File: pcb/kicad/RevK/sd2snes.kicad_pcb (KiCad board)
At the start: 2 copper layers, 101.5 x 83 mm, 148 parts, among them J101 SNESCART_EXT, J411 Hirose DM1AA, J421 USB Mini-B SMT, P113 CONN_1, P401 CONN_7X2, P402 CONN_2, P403 CONN_2, P404 CONN_3X2, Q101 2N2222A, Q301 IRLML6402PbF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

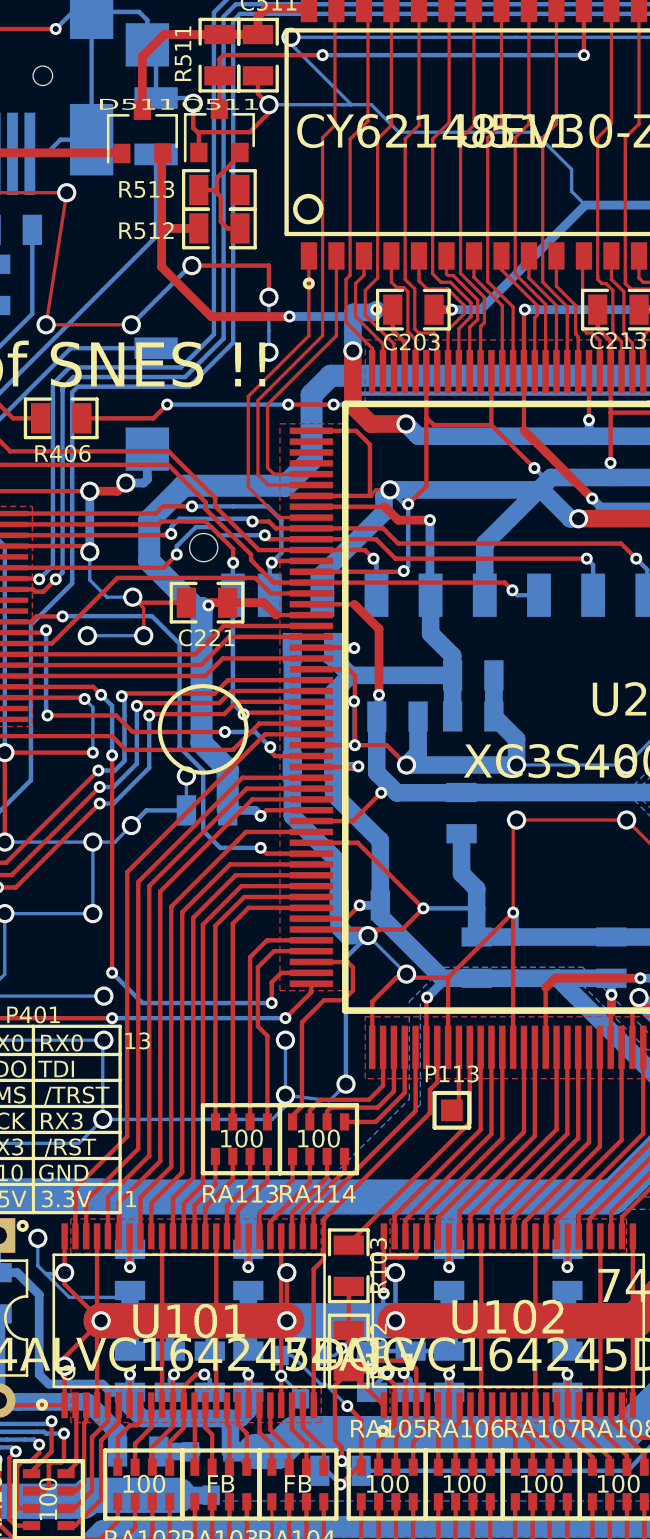
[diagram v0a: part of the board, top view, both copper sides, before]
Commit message: Fixes for Transistor placement
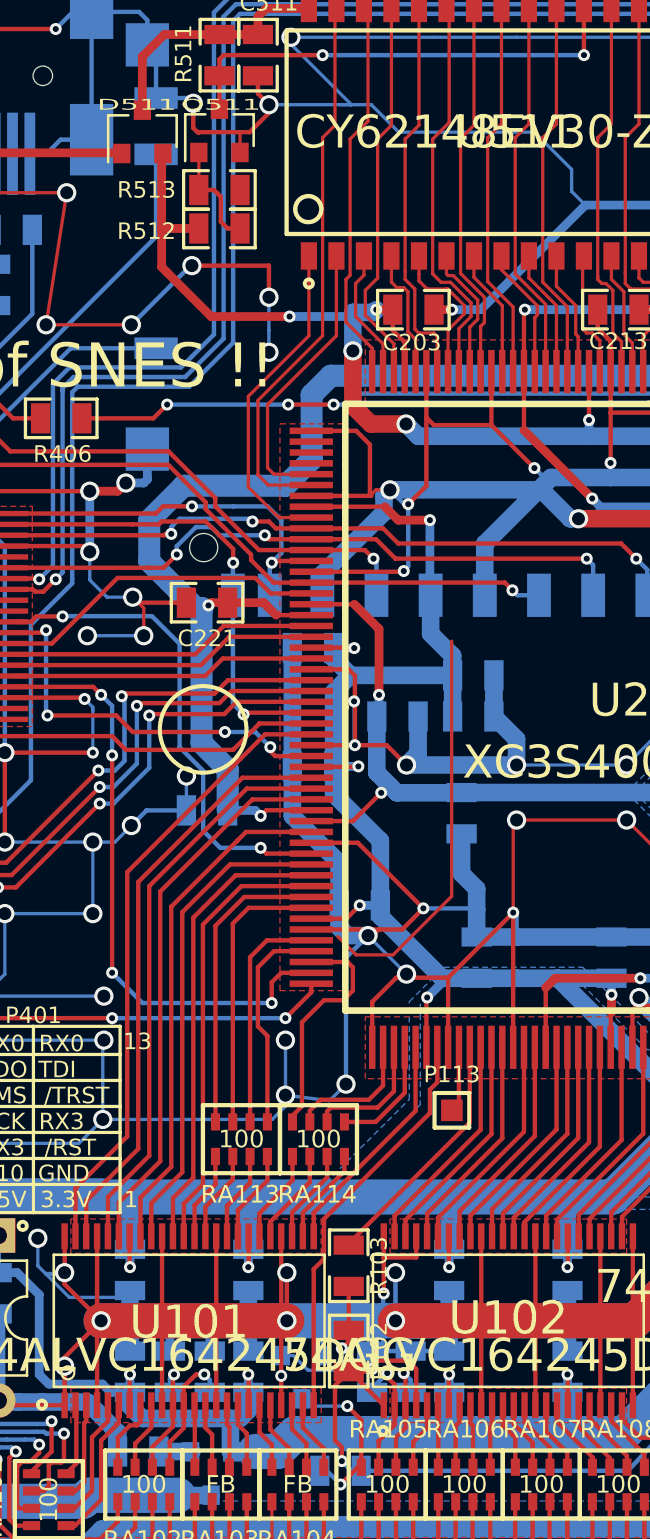
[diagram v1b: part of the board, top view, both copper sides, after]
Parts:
- moved Q101 0.06 mm to (142.5, 119.7)
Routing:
- net GND: track 1916.9 -> 1935.7 mm
- net Net-(Q101-Pad2): track 4.08 -> 6.89 mm
- net Net-(C123-Pad1): track 9.67 -> 8.00 mm
- net Net-(Q511-Pad2): track 5.66 -> 5.13 mm
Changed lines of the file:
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@@
     (thickness 0.8)
     (drawings 242)
-    (tracks 4097)
+    (tracks 4110)
     (zones 0)
     (modules 148)
@@
   )
   (layers
-    (0 Component signal)
-    (31 Copper signal hide)
+    (0 Component signal hide)
+    (31 Copper signal)
     (32 B.Adhes user hide)
     (33 F.Adhes user hide)
@@
   )
   (setup
-    (last_trace_width 0.2032)
+    (last_trace_width 0.1524)
     (user_trace_width 0.14986)
     (user_trace_width 0.1524)
@@
   )
   (module mypackages:SOT-23-EBC (layer Copper)
-    (at 142.4305 119.6975 270)
+    (at 142.494 119.6975 270)
     (descr "SOT-23, Standard")
     (tags SOT-23)
@@
   (segment (start 133.731 90.1065) (end 126.8095 90.1065) (width 0.2032) (layer Component) (net 86))
   (segment (start 142.9258 89.52484) (end 140.53058 89.52484) (width 0.2032) (layer Component) (net 86) (status 800))
+  (segment (start 144.994611 100.20299) (end 144.153891 99.36227) (width 0.1524) (layer Component) (net 87))
+  (segment (start 146.699033 100.20299) (end 144.994611 100.20299) (width 0.1524) (layer Component) (net 87))
+  (segment (start 149.4028 85.725) (end 149.4028 97.499223) (width 0.1524) (layer Component) (net 87))
+  (segment (start 149.4028 97.499223) (end 146.699033 100.20299) (width 0.1524) (layer Component) (net 87))
   (segment (start 119.888 127.6096) (end 132.4864 127.6096) (width 1.016) (layer Copper) (net 87))
   (segment (start 119.888 127.6096) (end 119.888 124.968) (width 1.016) (layer Component) (net 87))
@@
   (segment (start 101.9175 94.2975) (end 101.9175 99.568) (width 0.2032) (layer Component) (net 87))
   (via (at 118.364 113.03) (size 0.889) (drill 0.59944) (layers Component Copper) (net 87))
-  (segment (start 140.081 62.23) (end 139.3825 62.23) (width 0.2032) (layer Component) (net 87))
   (segment (start 99.1235 100.33) (end 97.79 100.33) (width 0.2032) (layer Component) (net 87) (status 400))
   (via (at 186.436 71.12) (size 0.889) (drill 0.59944) (layers Component Copper) (net 87))
@@
   (segment (start 120.8532 90.4875) (end 118.999 90.4875) (width 0.2032) (layer Component) (net 87))
   (segment (start 137.668 62.23) (end 137.734 62.296) (width 0.1524) (layer Component) (net 87))
-  (segment (start 137.734 63.23) (end 137.734 62.296) (width 0.2032) (layer Component) (net 87))
   (segment (start 141.53642 119.634) (end 141.53642 117.35308) (width 0.2032) (layer Component) (net 87) (status 800))
   (via (at 141.53642 119.634) (size 0.55372) (drill 0.29972) (layers Component Copper) (net 87))
-  (segment (start 142.4305 120.52808) (end 141.53642 119.634) (width 0.1524) (layer Copper) (net 87))
-  (segment (start 142.4305 120.6975) (end 142.4305 120.52808) (width 0.1524) (layer Copper) (net 87))
+  (segment (start 142.4305 120.6975) (end 142.4305 120.52808) (width 0.1524) (layer Copper) (net 306))
+  (segment (start 139.634 63.28) (end 139.634 63.23) (width 0.2032) (layer Component) (net 87))
+  (segment (start 139.6492 62.23) (end 139.3825 62.23) (width 0.2032) (layer Component) (net 87))
+  (segment (start 139.634 62.2452) (end 139.634 63.1665) (width 0.1524) (layer Component) (net 87))
+  (segment (start 139.6492 62.23) (end 139.634 62.2452) (width 0.1524) (layer Component) (net 87))
+  (segment (start 140.081 62.23) (end 139.6492 62.23) (width 0.2032) (layer Component) (net 87))
+  (segment (start 143.1925 117.8436) (end 143.1925 117.094) (width 0.1524) (layer Copper) (net 87))
+  (segment (start 143.444 118.0951) (end 143.1925 117.8436) (width 0.1524) (layer Copper) (net 87))
+  (segment (start 143.444 118.6975) (end 143.444 118.0951) (width 0.1524) (layer Copper) (net 87))
   (segment (start 130.683 85.217) (end 130.5687 85.3313) (width 0.2032) (layer Component) (net 88))
   (segment (start 130.7465 89.154) (end 130.683 89.0905) (width 0.2032) (layer Copper) (net 88))
@@
   (segment (start 138.5824 65.0494) (end 138.43 64.897) (width 0.2032) (layer Component) (net 305))
   (segment (start 138.7475 65.2145) (end 138.5824 65.0494) (width 0.2032) (layer Component) (net 305))
-  (segment (start 138.5824 64.3316) (end 139.634 63.28) (width 0.2032) (layer Component) (net 305))
-  (segment (start 139.634 63.28) (end 139.634 63.23) (width 0.2032) (layer Component) (net 305))
-  (segment (start 138.5824 65.0494) (end 138.5824 64.3316) (width 0.2032) (layer Component) (net 305))
+  (segment (start 137.734 64.8945) (end 137.7315 64.897) (width 0.1524) (layer Component) (net 305))
+  (segment (start 137.734 63.1665) (end 137.734 64.8945) (width 0.1524) (layer Component) (net 305))
   (segment (start 145.06956 123.85294) (end 145.23212 123.85294) (width 0.2032) (layer Component) (net 306))
   (segment (start 144.5895 121.031) (end 145.23212 121.67362) (width 0.2032) (layer Component) (net 306))
@@
   (segment (start 144.77238 124.15012) (end 145.06956 123.85294) (width 0.2032) (layer Component) (net 306))
   (via (at 144.5895 121.031) (size 0.55372) (layers Component Copper) (net 306))
-  (segment (start 142.0329 118.6975) (end 141.4805 118.6975) (width 0.1524) (layer Copper) (net 306))
-  (segment (start 143.354299 120.018899) (end 142.0329 118.6975) (width 0.1524) (layer Copper) (net 306))
-  (segment (start 143.577399 120.018899) (end 143.354299 120.018899) (width 0.1524) (layer Copper) (net 306))
-  (segment (start 144.5895 121.031) (end 143.577399 120.018899) (width 0.1524) (layer Copper) (net 306))
+  (segment (start 142.8275 121.031) (end 142.494 120.6975) (width 0.1524) (layer Copper) (net 306))
+  (segment (start 144.5895 121.031) (end 142.8275 121.031) (width 0.1524) (layer Copper) (net 306))
   (via (at 144.3355 118.364) (size 0.55372) (layers Component Copper) (net 307))
   (segment (start 144.653 118.0465) (end 144.653 117.5385) (width 0.2032) (layer Component) (net 307) (status 400))
   (segment (start 144.653 118.0465) (end 144.3355 118.364) (width 0.2032) (layer Component) (net 307))
   (segment (start 144.653 115.5065) (end 144.653 117.5385) (width 0.2032) (layer Component) (net 307) (status C00))
-  (segment (start 144.002 118.6975) (end 144.3355 118.364) (width 0.1524) (layer Copper) (net 307))
-  (segment (start 143.3805 118.6975) (end 144.002 118.6975) (width 0.1524) (layer Copper) (net 307))
+  (segment (start 144.3355 118.755539) (end 144.3355 118.364) (width 0.1524) (layer Copper) (net 307))
+  (segment (start 144.026881 119.376101) (end 144.3355 119.067482) (width 0.1524) (layer Copper) (net 307))
+  (segment (start 144.3355 119.067482) (end 144.3355 118.755539) (width 0.1524) (layer Copper) (net 307))
+  (segment (start 142.775001 119.376101) (end 144.026881 119.376101) (width 0.1524) (layer Copper) (net 307))
+  (segment (start 142.0964 118.6975) (end 142.775001 119.376101) (width 0.1524) (layer Copper) (net 307))
+  (segment (start 141.544 118.6975) (end 142.0964 118.6975) (width 0.1524) (layer Copper) (net 307))
   (segment (start 122.35942 105.66908) (end 122.35942 91.5797) (width 0.2032) (layer Component) (net 310) (status 400))
   (segment (start 121.7295 106.299) (end 122.35942 105.66908) (width 0.2032) (layer Component) (net 310))
@@
   (via (at 127.5715 75.2475) (size 0.55372) (layers Component Copper) (net 334))
   (segment (start 127.5715 75.2475) (end 126.1745 75.2475) (width 0.2032) (layer Component) (net 334))
-  (segment (start 101.944 111.9915) (end 101.444 111.9915) (width 0.2032) (layer Component) (net 344))
-  (segment (start 103.76916 107.6579) (end 103.76916 110.16634) (width 0.2032) (layer Component) (net 345))
-  (segment (start 105.26522 107.6579) (end 105.26522 111.49092) (width 0.2032) (layer Component) (net 346))
   (segment (start 106.299 115.4303) (end 106.299 116.332) (width 0.2032) (layer Component) (net 343))
   (segment (start 108.310202 112.701202) (end 108.259401 112.650401) (width 0.2032) (layer Component) (net 343))
@@
   (segment (start 107.258504 115.4303) (end 108.310202 114.378602) (width 0.2032) (layer Component) (net 343))
   (segment (start 106.299 115.4303) (end 107.258504 115.4303) (width 0.2032) (layer Component) (net 343))
+  (segment (start 101.944 111.9915) (end 101.444 111.9915) (width 0.2032) (layer Component) (net 344))
   (segment (start 100.584 116.078) (end 100.584 116.332) (width 0.2032) (layer Component) (net 344))
   (segment (start 102.423001 114.492999) (end 100.584 116.332) (width 0.2032) (layer Component) (net 344))
@@
   (segment (start 102.423001 112.064001) (end 102.359401 112.000401) (width 0.2032) (layer Component) (net 344))
   (segment (start 102.423001 114.492999) (end 102.423001 112.064001) (width 0.2032) (layer Component) (net 344))
+  (segment (start 103.76916 107.6579) (end 103.76916 110.16634) (width 0.2032) (layer Component) (net 345))
   (segment (start 101.431201 113.300401) (end 101.431201 112.650401) (width 0.2032) (layer Component) (net 345))
   (segment (start 101.94906 110.16634) (end 103.76916 110.16634) (width 0.2032) (layer Component) (net 345))
@@
   (segment (start 100.503001 112.650401) (end 100.4522 112.5996) (width 0.2032) (layer Component) (net 345))
   (segment (start 101.431201 112.650401) (end 100.503001 112.650401) (width 0.2032) (layer Component) (net 345))
+  (segment (start 105.26522 107.6579) (end 105.26522 111.49092) (width 0.2032) (layer Component) (net 346))
   (segment (start 107.331201 113.950401) (end 107.331201 113.300401) (width 0.2032) (layer Component) (net 346))
   (segment (start 106.403001 113.300401) (end 105.26522 112.16262) (width 0.2032) (layer Component) (net 346))

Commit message: Fix stupid layout mistake
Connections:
- U230 pad 2: Net-(U230-Pad2) -> Net-(R231-Pad1)
- U230 pad 3: Net-(U230-Pad2) -> Net-(U230-Pad3)
- U230 pad 6: Net-(U230-Pad5) -> Net-(R230-Pad1)
- U341 pad 7: Net-(U230-Pad2) -> Net-(U230-Pad3)
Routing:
- net Net-(U230-Pad2): track 9.03 -> 0.00 mm
- net Net-(U230-Pad3): track 0.00 -> 7.15 mm
- net GNDA: track 106.7 -> 104.5 mm
- net Net-(R231-Pad1): track 6.80 -> 6.18 mm

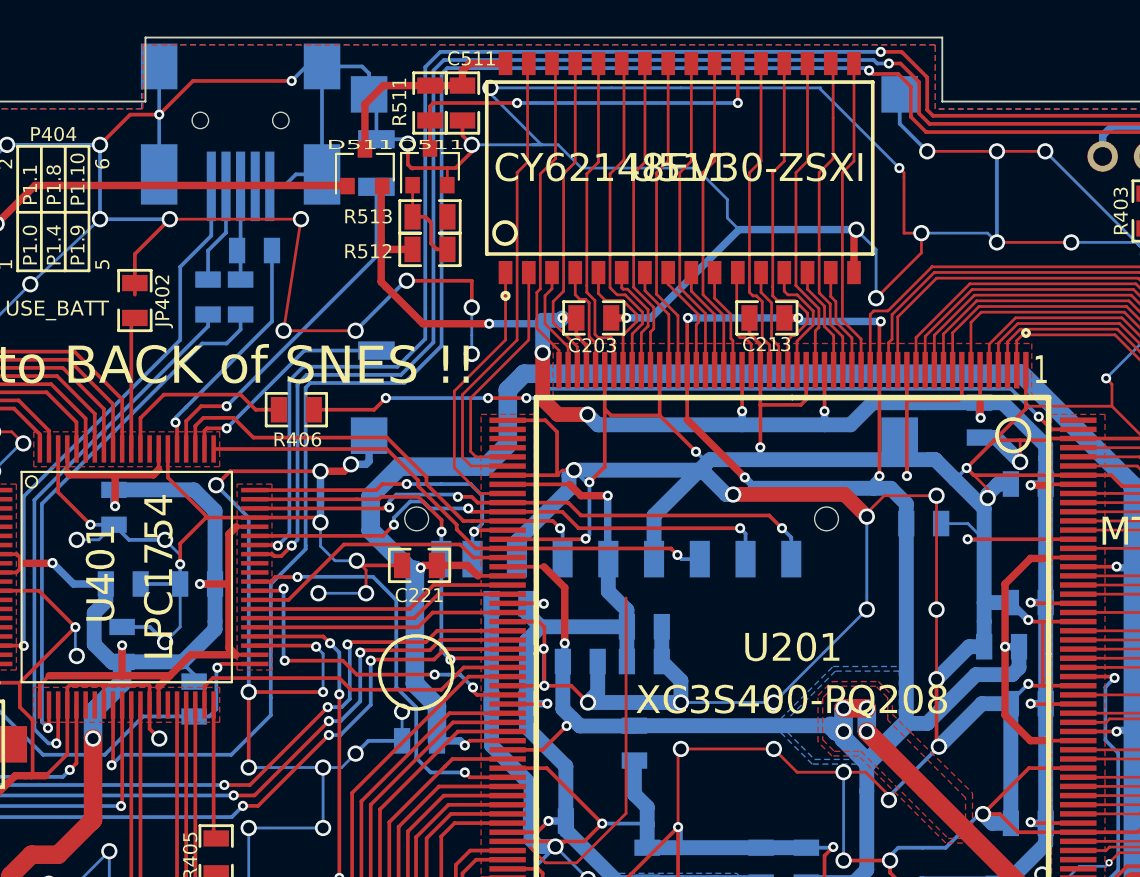
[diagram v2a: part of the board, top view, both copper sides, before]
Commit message: - Reroute to use small SD card slot
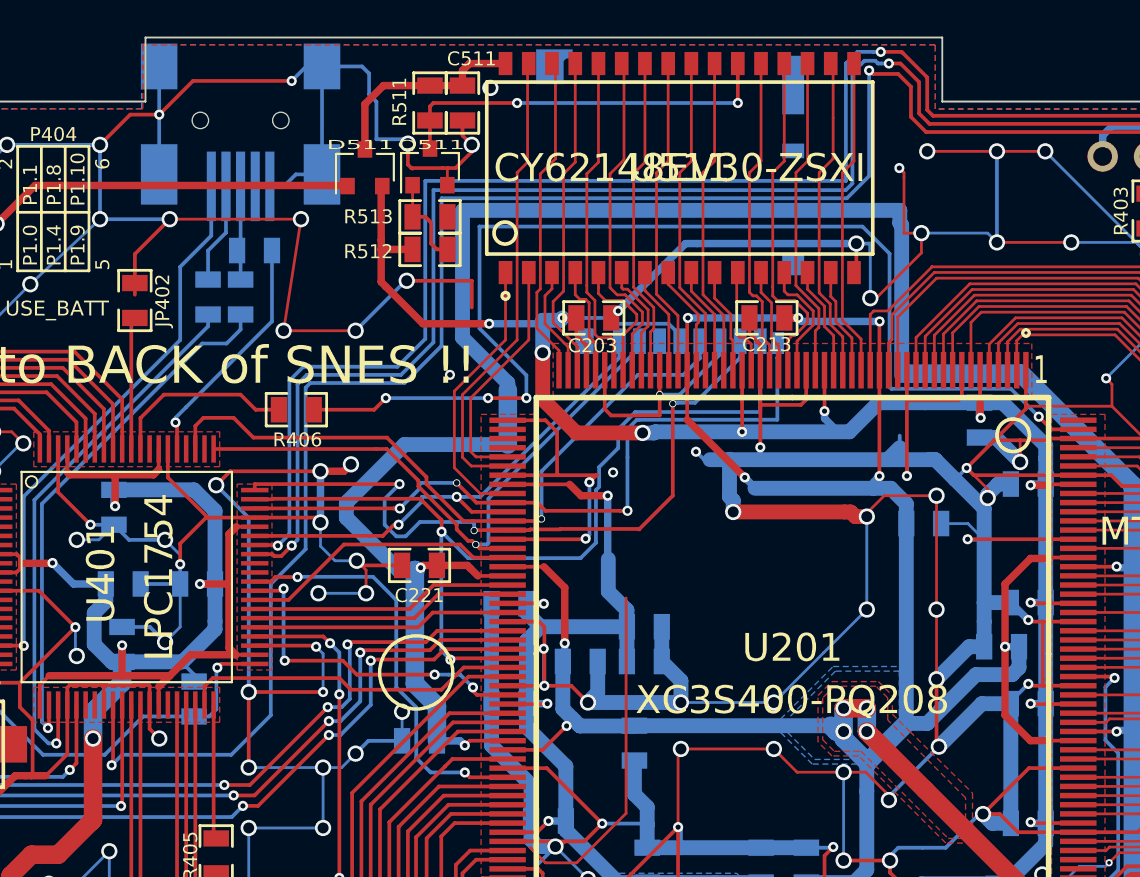
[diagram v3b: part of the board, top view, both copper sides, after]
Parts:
- J411: footprint mypackages:HRS-DM1AA -> Connectors_Card:Hirose_DM3BT-DSF-PEJS
- moved J411 2.43 mm to (149.0, 71.0)
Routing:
- net GND: track 1935.7 -> 1857.4 mm
- net SD_DAT1: track 21.8 -> 49.8 mm
- net +1.2V: track 115.5 -> 139.2 mm
- net SD_DAT0: track 18.4 -> 39.4 mm, vias 2 -> 3
- net PROG_B: track 43.2 -> 64.0 mm
- net Net-(J411-PadWP): track 19.5 -> 0.00 mm, vias 1 -> 0
- net Net-(J411-PadDT): track 12.2 -> 0.00 mm, vias 1 -> 0
- net SD_CLK: track 25.8 -> 37.7 mm
- net +3.3V: track 549.1 -> 558.2 mm
- net SD_DAT2: track 32.0 -> 38.8 mm
- net SD_CMD: track 29.4 -> 33.8 mm
- net SD_DAT3: track 29.9 -> 27.9 mm, vias 3 -> 2
- net Net-(R403-Pad1): track 104.2 -> 103.6 mm
